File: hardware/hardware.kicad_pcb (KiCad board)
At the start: 2 copper layers, 55 parts, among them J1 BATT, J2 RFID-RC522, J4 PROG, J5 EXT, J6 PCM5102A_1, J7 PCM5102A_2, J8 Speakers, J9 CHARGER, SW1 Vol down, SW2 Vol up, SW3 Trk next, SW4 Trk prev, SW5 Reset, U1 ESP32-WROOM-32, U2 XRP6272, U3 XRP6272, U4 PAM8403

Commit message: [wip] board layout
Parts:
- added J3: 104031-0811, SDSlot:1040310811, F.Cu at (33.0, 123.2)
- J2: footprint Connector_PinSocket_2.54mm:PinSocket_1x08_P2.54mm_Vertical -> RFID-RC522:RFID-RC522-Module
- moved C9 182.4 mm to (109.2, 119.4)
- moved J8 180.0 mm to (104.1, 115.6), turned to 270 degrees
- moved L1 177.0 mm to (110.5, 100.3)
- moved R5 167.3 mm to (28.4, 106.7)
- moved J7 164.5 mm to (63.5, 101.6)
- moved R13 152.5 mm to (58.0, 119.4)
- moved SW1 152.3 mm to (76.2, 114.3)
- moved C8 151.1 mm to (100.3, 100.3)
- moved U4 149.2 mm to (90.2, 105.4), turned to 90 degrees
- moved U3 145.9 mm to (55.0, 102.9)
- moved R2 143.8 mm to (33.5, 106.7)
- moved R14 143.7 mm to (52.9, 120.7)
- moved J1 143.4 mm to (109.2, 87.6)
- moved J9 141.8 mm to (115.6, 87.6)
- moved R18 140.2 mm to (52.1, 113.0)
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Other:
- board outline added: 101.6 x 101.6 mm

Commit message: [wip] board layout
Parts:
- moved C16 161.5 mm to (76.2, 123.2)
- moved C10 153.0 mm to (94.0, 119.4)
- moved C15 144.3 mm to (74.9, 106.7), turned to 180 degrees
- moved C14 138.1 mm to (83.8, 111.7), turned to 90 degrees
- moved C11 138.0 mm to (95.2, 101.6)
- moved C13 138.0 mm to (88.9, 101.6)
- moved C12 127.1 mm to (35.6, 103.1), turned to 270 degrees
- moved C17 121.4 mm to (35.6, 96.7), turned to 270 degrees
- moved C5 111.2 mm to (94.2, 81.3), turned to 225 degrees
- moved C7 109.8 mm to (40.9, 90.2), turned to 180 degrees
- moved C3 102.2 mm to (108.0, 62.2), turned to 90 degrees
- moved J3 94.2 mm to (49.5, 30.5), turned to 180 degrees
- moved C6 87.7 mm to (44.5, 62.0), turned to 90 degrees
- moved C4 85.2 mm to (44.5, 69.6), turned to 270 degrees
- moved J5 74.0 mm to (101.6, 83.8), turned to 315 degrees
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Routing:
- net +BATT: track 0.00 -> 228.8 mm
- net +5VA: track 0.00 -> 73.7 mm
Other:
- net class Default: clearance 0.2 -> 0.3; trace_width 0.25 -> 0.4; via_dia 0.8 -> 1.5; via_drill 0.4 -> 0.8
- net class Power added: clearance 0.3, trace_width 1, via_dia 2, via_drill 0.8
- rule trace_clearance: 0.2 -> 0.3

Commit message: [wip] routing...
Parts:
- C10, C11, C12, C13, C14, C15, C16, C17, C2, C5, C7, C8, C9, J1, J5, J8, J9, L1, R11, R13, R14, R17, R18, R9, U1, U3: moved to B.Cu
- moved C5 45.9 mm to (75.7, 39.2), turned to 90 degrees
- moved R11 41.9 mm to (49.7, 56.0)
- moved R9 41.5 mm to (80.4, 41.0), turned to 90 degrees
- moved R19 31.8 mm to (89.5, 119.4)
- moved U1 30.9 mm to (63.5, 47.0), turned to 180 degrees
- moved R14 30.7 mm to (58.0, 94.0)
- moved C3 28.9 mm to (86.0, 43.4)
- moved R7 22.0 mm to (110.4, 44.8)
- moved R8 21.0 mm to (110.4, 40.7)
- moved R17 20.2 mm to (31.4, 99.5), turned to 90 degrees
- moved R3 18.8 mm to (50.6, 44.6)
- moved J5 18.0 mm to (92.7, 68.2), turned to 90 degrees
- moved R1 16.5 mm to (46.6, 44.6)
- moved R6 14.4 mm to (42.4, 44.6)
- moved R18 13.1 mm to (35.9, 101.4), turned to 90 degrees
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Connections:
- J2 pad 5: Net-(J2-Pad5) -> (no net)
- J3 pad 10: Net-(J3-Pad10) -> (no net)
- J3 pad 9: Net-(J3-Pad9) -> (no net)
- J7 pad 1: Net-(J7-Pad1) -> (no net)
- J7 pad 2: Net-(J7-Pad2) -> (no net)
- J7 pad 3: Net-(J7-Pad3) -> (no net)
- J7 pad 5: Net-(J7-Pad5) -> (no net)
- J7 pad 6: Net-(J7-Pad6) -> (no net)
- J8 pad 3: Net-(J8-Pad3) -> (no net)
- L1 pad 1: +BATT -> GNDD
- L1 pad 2: +5VA -> GNDA
- L1 pad 3: GNDD -> +BATT
- L1 pad 4: GNDA -> +5VA
- U1 pad 17: Net-(U1-Pad17) -> (no net)
- U1 pad 18: Net-(U1-Pad18) -> (no net)
- U1 pad 19: Net-(U1-Pad19) -> (no net)
- U1 pad 20: Net-(U1-Pad20) -> (no net)
- U1 pad 21: Net-(U1-Pad21) -> (no net)
- U1 pad 22: Net-(U1-Pad22) -> (no net)
- U1 pad 32: Net-(U1-Pad32) -> (no net)
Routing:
- net GNDD: track 0.00 -> 494.0 mm, vias 0 -> 4
- net +3V3: track 0.00 -> 219.6 mm, vias 0 -> 2
- net +BATT: track 228.8 -> 417.4 mm
- net /AMP_ENA: track 0.00 -> 172.3 mm, vias 0 -> 3
- net /POWER_CTRL: track 0.00 -> 151.4 mm, vias 0 -> 2
- net GNDA: track 0.00 -> 142.2 mm, vias 0 -> 4
- net /TRK_NEXT: track 0.00 -> 140.7 mm, vias 0 -> 1
- net /VOL_DOWN: track 0.00 -> 130.3 mm, vias 0 -> 1
- net /RFID-SDA: track 0.00 -> 82.7 mm, vias 0 -> 2
- net /I2S_LRCK: track 0.00 -> 77.5 mm
- net /RFID-MISO: track 0.00 -> 66.9 mm, vias 0 -> 2
- net +3.3VDAC: track 0.00 -> 66.5 mm, vias 0 -> 2
- net /EXT3: track 0.00 -> 66.5 mm, vias 0 -> 2
- net /I2S_BCK: track 0.00 -> 58.7 mm
- net /DTR: track 0.00 -> 58.5 mm, vias 0 -> 2
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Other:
- net class Default: via_drill 0.8 -> 0.5
- net class Power: trace_width 1 -> 0.8; via_drill 0.8 -> 0.5
- net class Power D added: clearance 0.3, trace_width 0.6, via_dia 2, via_drill 0.5

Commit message: PBC routing complete
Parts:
- moved C16 19.3 mm to (57.1, 120.4)
- moved R16 18.0 mm to (65.6, 118.6)
- moved C15 17.6 mm to (59.6, 115.3)
- moved R15 14.9 mm to (65.6, 110.5)
- moved R13 11.5 mm to (58.3, 104.6), turned to 90 degrees
- moved J5 8.91 mm to (92.1, 59.3)
- moved C12 1.57 mm to (35.6, 105.8)
- moved C17 1.57 mm to (31.1, 103.4)
- moved C7 1.57 mm to (40.5, 88.6)
- moved J6 1.57 mm to (52.3, 93.7)
- moved J7 1.57 mm to (53.0, 100.1)
- moved R14 1.57 mm to (57.7, 92.5)
- moved R17 1.57 mm to (31.0, 98.0)
- moved U3 1.57 mm to (44.4, 102.1)
- moved R18 1.57 mm to (35.6, 99.9)
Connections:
- net Net-(J8-Pad1) renamed /SR+
- net Net-(J8-Pad2) renamed /SR-
- net Net-(J8-Pad4) renamed /SL-
- net Net-(J8-Pad5) renamed /SL+
- J8 pad 3: (no net) -> GNDA
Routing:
- net GNDD: track 494.0 -> 1285.6 mm, vias 4 -> 11
- net GNDA: track 142.2 -> 420.0 mm, vias 4 -> 5
- net +BATT: track 417.4 -> 229.7 mm
- net +5VA: track 122.4 -> 210.0 mm, vias 0 -> 2
- net +3V3: track 219.6 -> 290.6 mm, vias 2 -> 5
- net /POWER_CTRL: track 151.4 -> 194.8 mm
- net /VOL_DOWN: track 130.3 -> 158.0 mm
- net /EXT3: track 66.5 -> 39.4 mm, vias 2 -> 1
- net Net-(R16-Pad2): track 11.8 -> 34.5 mm
- net /L: track 23.3 -> 4.10 mm, vias 1 -> 0
- net /R: track 23.4 -> 4.37 mm, vias 1 -> 0
- net /TRK_PREV: track 35.5 -> 54.3 mm
- net Net-(R15-Pad2): track 10.1 -> 25.9 mm
- net /EXT1: track 57.2 -> 42.1 mm, vias 2 -> 1
- net /TRK_NEXT: track 140.7 -> 127.3 mm
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- added copper zone on B.Cu, net GNDA
- added copper zone on F.Cu, net GNDA
- added copper zone on B.Cu, net GNDD
- added copper zone on F.Cu, net GNDD
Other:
- net class Default: clearance 0.3 -> 0.2
- net class Power: clearance 0.3 -> 0.2
- net class Power D: clearance 0.3 -> 0.2
- net class Speaker added: clearance 0.2, trace_width 0.8, via_dia 2, via_drill 0.5
- rule trace_clearance: 0.3 -> 0.2

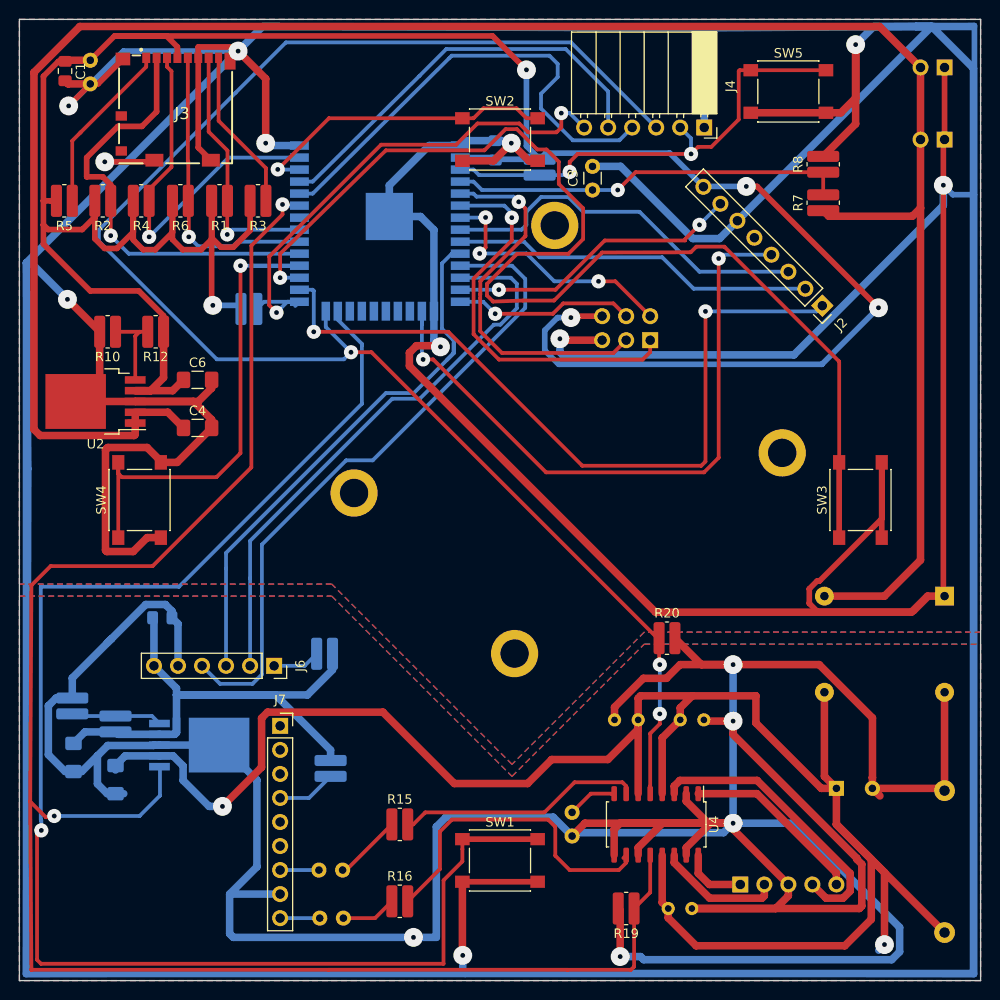
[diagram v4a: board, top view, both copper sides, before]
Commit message: corrections to PCB, started 3D model
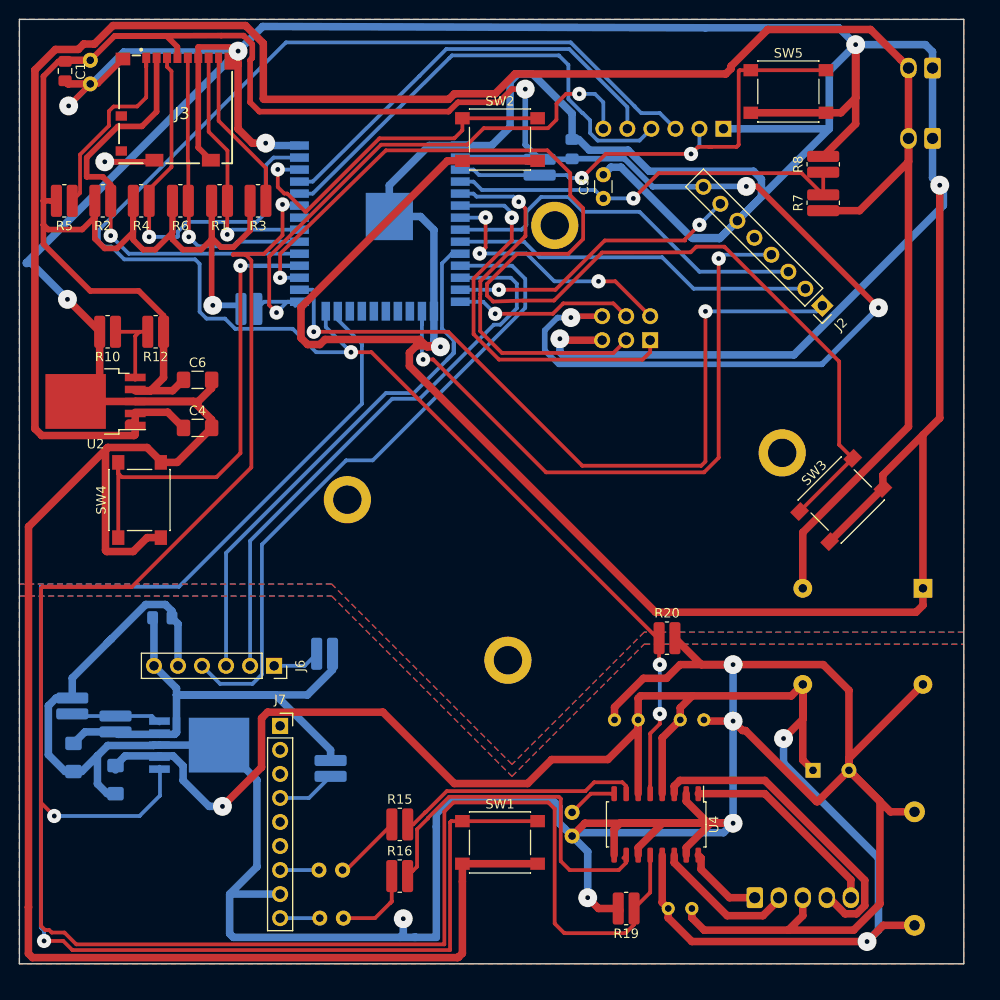
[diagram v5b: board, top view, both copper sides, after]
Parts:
- C9: footprint Capacitor_THT:C_Rect_L16.5mm_W4.7mm_P15.00mm_MKT -> Capacitor_THT:C_Rect_L16.5mm_W4.7mm_P12.00mm_MKT
- J1, J9: footprint Connector_PinHeader_2.54mm:PinHeader_1x02_P2.54mm_Vertical -> Connector_Molex:Molex_KK-254_AE-6410-02A_1x02_P2.54mm_Vertical
- J4: footprint Connector_PinSocket_2.54mm:PinSocket_1x06_P2.54mm_Horizontal -> Connector_PinHeader_2.54mm:PinHeader_1x06_P2.54mm_Horizontal; moved to B.Cu
- J8: footprint Connector_PinHeader_2.54mm:PinHeader_1x05_P2.54mm_Horizontal -> Connector_Molex:Molex_KK-254_AE-6410-05A_1x05_P2.54mm_Vertical
- U2, U3: footprint Package_TO_SOT_SMD:TO-252-5_TabPin3 -> SDSlot:TO-252-5_TabPin3_127
- moved C5 8.13 mm to (83.8, 39.1)
- moved C9 3.27 mm to (120.0, 121.2)
- moved C8 3.12 mm to (109.3, 104.8)
- moved R16 2.67 mm to (65.6, 116.0)
- moved L1 2.43 mm to (120.9, 85.5)
- moved J8 2.07 mm to (103.1, 118.2), turned to 0 degrees
- moved J4 2.04 mm to (99.8, 37.0), turned to 90 degrees
- moved SW3 2.03 mm to (112.3, 76.2), turned to 45 degrees
- moved SW1 1.91 mm to (76.2, 112.4)
- moved C3 1.45 mm to (87.1, 44.3)
- moved J9 1.28 mm to (121.9, 38.0), turned to 180 degrees
- moved J1 1.27 mm to (121.9, 30.5), turned to 180 degrees
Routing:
- net GNDD: track 1285.6 -> 845.3 mm, vias 11 -> 9
- net GNDA: track 420.0 -> 371.3 mm
- net +5VA: track 210.0 -> 189.5 mm, vias 2 -> 3
- net /POWER_CTRL: track 194.8 -> 215.0 mm
- net +BATT: track 229.7 -> 236.8 mm
- net +3V3: track 290.6 -> 296.6 mm
- net /DTR: track 56.4 -> 61.4 mm
- net /VOL_UP: track 32.9 -> 37.5 mm
- net /AMP_ENA: track 171.8 -> 176.2 mm
- net /SD-MOSI: track 38.2 -> 41.5 mm
- net /SL-: track 30.5 -> 33.6 mm
- net Net-(R16-Pad2): track 34.5 -> 37.5 mm
- net Net-(C16-Pad2): track 5.86 -> 8.79 mm
- net /SL+: track 19.3 -> 21.8 mm
- net /SR-: track 13.2 -> 15.1 mm
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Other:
- board size 101.6 x 101.6 mm -> 99.8 x 99.8 mm
- rule trace_min: 0.2 -> 0.4
- rule via_min_size: 0.4 -> 1

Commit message: finalize PCB
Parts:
- added REF**: MountingHole_3.2mm_M3_Pad, MountingHole:MountingHole_3.2mm_M3_Pad, F.Cu at (120.4, 30.2)
- added REF**: MountingHole_3.2mm_M3_Pad, MountingHole:MountingHole_3.2mm_M3_Pad, F.Cu at (30.4, 30.2)
- added REF**: MountingHole_3.2mm_M3_Pad, MountingHole:MountingHole_3.2mm_M3_Pad, F.Cu at (30.4, 120.2)
- added REF**: MountingHole_3.2mm_M3_Pad, MountingHole:MountingHole_3.2mm_M3_Pad, F.Cu at (120.4, 120.2)
- C9: footprint Capacitor_THT:C_Rect_L16.5mm_W4.7mm_P12.00mm_MKT -> Capacitor_THT:C_Rect_L16.5mm_W8.7mm_P15.00mm_MKT; moved to F.Cu
- J4: footprint Connector_PinHeader_2.54mm:PinHeader_1x06_P2.54mm_Horizontal -> Connector_Molex:Molex_KK-254_AE-6410-06A_1x06_P2.54mm_Vertical; moved to F.Cu
- SW1: value Vol down -> Trk next
- SW2: value Vol up -> Trk prev
- SW3: value Trk next -> Vol up
- SW4: value Trk prev -> Vol down
- U2, U3: footprint SDSlot:TO-252-5_TabPin3_127 -> Package_TO_SOT_SMD:TO-252-5_TabPin3
- moved C1 90.6 mm to (36.3, 121.2), turned to 0 degrees
- moved C2 89.1 mm to (34.9, 118.8), turned to 0 degrees
- moved C9 88.9 mm to (114.9, 32.4), turned to 180 degrees
- moved J3 80.5 mm to (29.2, 108.7), turned to 270 degrees
- moved J9 77.4 mm to (45.1, 28.6), turned to 270 degrees
- moved R5 77.3 mm to (44.6, 120.5), turned to 270 degrees
- moved SW5 74.5 mm to (33.0, 43.9), turned to 90 degrees
- moved C17 74.1 mm to (103.4, 119.5), turned to 0 degrees
- moved R2 72.6 mm to (44.6, 116.4), turned to 270 degrees
- moved J8 72.3 mm to (118.2, 47.5), turned to 90 degrees
- moved C12 70.8 mm to (105.8, 115.1), turned to 0 degrees
- moved R17 70.4 mm to (98.0, 119.6), turned to 180 degrees
- moved R8 69.6 mm to (40.7, 40.3), turned to 180 degrees
- moved C16 68.7 mm to (120.4, 93.5), turned to 90 degrees
- moved R4 68.1 mm to (44.6, 112.3), turned to 270 degrees
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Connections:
- J2 pad 5: (no net) -> Net-(J2-Pad5)
- J3 pad 10: (no net) -> Net-(J3-Pad10)
- J3 pad 9: (no net) -> Net-(J3-Pad9)
- J7 pad 1: (no net) -> Net-(J7-Pad1)
- J7 pad 2: (no net) -> Net-(J7-Pad2)
- J7 pad 3: (no net) -> Net-(J7-Pad3)
- J7 pad 5: (no net) -> Net-(J7-Pad5)
- J7 pad 6: (no net) -> Net-(J7-Pad6)
- SW1 pad 1: /VOL_DOWN -> /TRK_NEXT
- SW2 pad 1: /VOL_UP -> /TRK_PREV
- SW3 pad 1: /TRK_NEXT -> /VOL_UP
- SW4 pad 1: /TRK_PREV -> /VOL_DOWN
- U1 pad 17: (no net) -> Net-(U1-Pad17)
- U1 pad 18: (no net) -> Net-(U1-Pad18)
- U1 pad 19: (no net) -> Net-(U1-Pad19)
- U1 pad 20: (no net) -> Net-(U1-Pad20)
- U1 pad 21: (no net) -> Net-(U1-Pad21)
- U1 pad 22: (no net) -> Net-(U1-Pad22)
- U1 pad 23: /VOL_DOWN -> /TRK_NEXT
- U1 pad 27: /TRK_NEXT -> /VOL_UP
- U1 pad 28: /TRK_PREV -> /VOL_DOWN
- U1 pad 32: (no net) -> Net-(U1-Pad32)
- U1 pad 36: /VOL_UP -> /TRK_PREV
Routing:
- net /VOL_DOWN: track 156.5 -> 54.3 mm
- net /VOL_UP: track 37.5 -> 125.6 mm
- net GNDA: track 371.3 -> 400.6 mm, vias 5 -> 2
- net /TRK_NEXT: track 125.6 -> 144.8 mm
- net /TRK_PREV: track 54.3 -> 37.5 mm
- net +5VA: track 189.5 -> 204.8 mm, vias 3 -> 2
- net /POWER_CTRL: track 215.0 -> 202.9 mm
- net GNDD: track 845.3 -> 840.1 mm
- net +BATT: track 236.8 -> 233.9 mm
- net /AMP_ENA: track 176.2 -> 178.3 mm
- net Net-(R16-Pad2): track 37.5 -> 36.2 mm
- net /I2S_LRCK: track 70.0 -> 70.8 mm
- net Net-(R15-Pad2): track 25.9 -> 26.7 mm
- net /SL+: track 21.8 -> 22.4 mm

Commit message: update 3D model and PCB
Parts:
- moved J5 4.13 mm to (62.1, 55.5)
- moved C3 2.47 mm to (46.1, 61.8)
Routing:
- net GNDD: track 840.1 -> 598.3 mm, vias 9 -> 7
- net GNDA: track 400.6 -> 287.0 mm, vias 2 -> 4
- net /AMP_ENA: track 178.3 -> 137.5 mm
- net /TRK_NEXT: track 144.8 -> 175.6 mm
- net +3V3: track 296.3 -> 271.9 mm, vias 5 -> 3
- net /TRK_PREV: track 37.5 -> 55.1 mm
- net Net-(R15-Pad2): track 26.7 -> 43.7 mm
- net /RFID-RST: track 31.3 -> 47.7 mm
- net /EXT2: track 27.5 -> 43.6 mm, vias 3 -> 1
- net /RFID-MISO: track 70.2 -> 54.9 mm
- net /EXT3: track 39.4 -> 53.5 mm
- net /RFID-SDA: track 82.7 -> 72.2 mm, vias 2 -> 0
- net +5VA: track 204.8 -> 195.9 mm
- net /RESET: track 51.6 -> 60.4 mm
- net +BATT: track 233.9 -> 225.7 mm
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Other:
- net class Default: clearance 0.2 -> 0.25; trace_width 0.4 -> 0.6; via_dia 1.5 -> 2
- net class Power: clearance 0.2 -> 0.25
- net class Power D: clearance 0.2 -> 0.25; trace_width 0.6 -> 0.8
- net class Speaker: clearance 0.2 -> 0.25
- rule trace_clearance: 0.2 -> 0.25

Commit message: adjustments: reroute tracks to keep-out antenna add optional pin headers below/close to buttons for external push buttons minor cleanup
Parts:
- added J10: Trk next, Connector_PinHeader_2.54mm:PinHeader_1x02_P2.54mm_Vertical, B.Cu at (118.7, 73.8)
- added J11: Trk prev, Connector_PinHeader_2.54mm:PinHeader_1x02_P2.54mm_Vertical, B.Cu at (31.3, 69.3)
- added J12: Vol up, Connector_PinHeader_2.54mm:PinHeader_1x02_P2.54mm_Vertical, B.Cu at (68.5, 37.0)
- added J13: Vol down, Connector_PinHeader_2.54mm:PinHeader_1x02_P2.54mm_Vertical, B.Cu at (75.5, 113.7)
- added J14: Reset, Connector_PinHeader_2.54mm:PinHeader_1x02_P2.54mm_Vertical, B.Cu at (31.8, 44.1)
- moved SW1 7.76 mm to (120.1, 74.0)
- moved J4 6.72 mm to (30.2, 51.6)
- moved L1 4.06 mm to (85.5, 33.8)
- moved J6 4.06 mm to (89.7, 98.3)
- moved J7 4.06 mm to (96.0, 97.7)
- moved C8 3.81 mm to (104.6, 40.6), turned to -90 degrees
- moved C7 3.68 mm to (88.5, 113.8), turned to 0 degrees
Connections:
- J2 pad 5: Net-(J2-Pad5) -> unconnected-(J2-Pad5)
- J3 pad 10: Net-(J3-Pad10) -> unconnected-(J3-Pad10)
- J3 pad 9: Net-(J3-Pad9) -> unconnected-(J3-Pad9)
- J7 pad 1: Net-(J7-Pad1) -> unconnected-(J7-Pad1)
- J7 pad 2: Net-(J7-Pad2) -> unconnected-(J7-Pad2)
- J7 pad 3: Net-(J7-Pad3) -> unconnected-(J7-Pad3)
- J7 pad 5: Net-(J7-Pad5) -> unconnected-(J7-Pad5)
- J7 pad 6: Net-(J7-Pad6) -> unconnected-(J7-Pad6)
- R19 pad 1: /POWER_CTRL -> /AMP_ENA
- U1 pad 17: Net-(U1-Pad17) -> unconnected-(U1-Pad17)
- U1 pad 18: Net-(U1-Pad18) -> unconnected-(U1-Pad18)
- U1 pad 19: Net-(U1-Pad19) -> unconnected-(U1-Pad19)
- U1 pad 20: Net-(U1-Pad20) -> unconnected-(U1-Pad20)
- U1 pad 21: Net-(U1-Pad21) -> unconnected-(U1-Pad21)
- U1 pad 22: Net-(U1-Pad22) -> unconnected-(U1-Pad22)
- U1 pad 32: Net-(U1-Pad32) -> unconnected-(U1-Pad32)
- U1 pad 33: /POWER_CTRL -> /AMP_ENA
- U3 pad 1: /POWER_CTRL -> /AMP_ENA
- U4 pad 12: /POWER_CTRL -> /AMP_ENA
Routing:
- net GNDD: track 598.3 -> 801.5 mm, vias 7 -> 4
- net /POWER_CTRL: track 200.0 -> 0.00 mm, vias 1 -> 0
- net /AMP_ENA: track 137.5 -> 334.3 mm, vias 3 -> 2
- net +BATT: track 225.7 -> 131.6 mm, vias 0 -> 1
- net /TRK_NEXT: track 175.6 -> 147.4 mm
- net /VOL_UP: track 125.2 -> 100.9 mm
- net Net-(R15-Pad2): track 43.7 -> 26.0 mm
- net +3V3: track 271.9 -> 254.7 mm
- net +5VA: track 195.9 -> 184.9 mm, vias 2 -> 1
- net /TX: track 48.2 -> 58.8 mm, vias 2 -> 0
- net /RX: track 47.2 -> 56.4 mm
- net /RFID-RST: track 47.7 -> 39.2 mm
- net Net-(R16-Pad2): track 34.0 -> 25.5 mm
- net /RESET: track 60.4 -> 53.3 mm, vias 2 -> 1
- net /VOL_DOWN: track 54.4 -> 47.4 mm
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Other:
- net class Default removed
- net class Power removed
- net class Power D removed
- net class Speaker removed
